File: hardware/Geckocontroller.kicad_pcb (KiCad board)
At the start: 2 copper layers, 114.3 x 96.5 mm, 103 parts, among them J101 AC Input, J11 I²C (BME280), J21 RGB LED, J31 DS18B20 I, J32 DS18B20 II, J40 FAN, J51 USB-C, J60 Load Cell Connector, J70 SPI / Addon Connector, J81 Dimmer, J91 Pump, J92 HeatBed, J93 HeatLamp, K81 AQG12212, K91 AQG12112, K92 AQG12112, K93 AQG12112, Q21 AO3400A, Q22 AO3400A, Q23 AO3400A, Q51 S8050, Q52 S8050, Q61 S8550, Q81 AO3400A, Q91 AO3400A, Q92 AO3400A, Q93 AO3400A, SW1 SW_Push, SW2 SW_Push, U1 ESP32-WROOM-32, U101 ACT4088, U2 CP2102, U61 HX711, U81 6N138

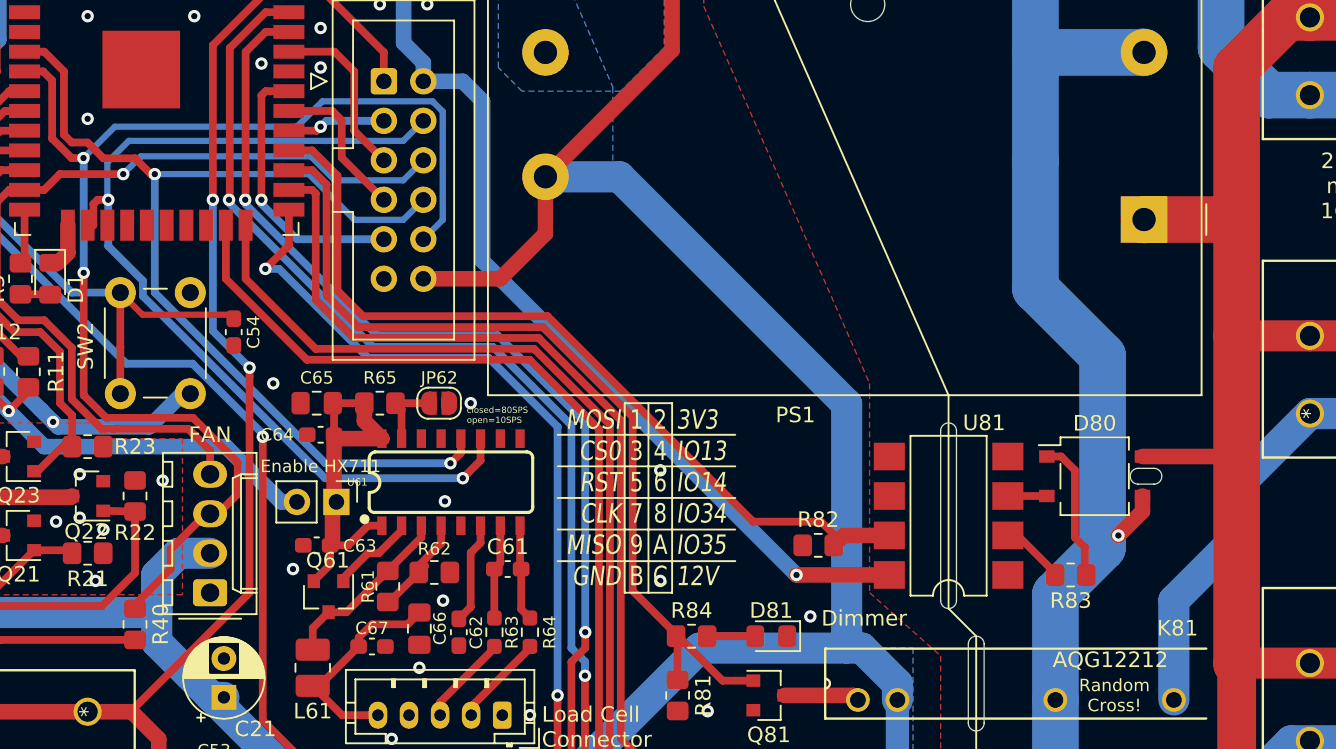
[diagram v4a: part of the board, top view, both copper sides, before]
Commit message: hardware: Improve Zero-Cross Detection circuit
Thanks to Patagona and LeoDJ!
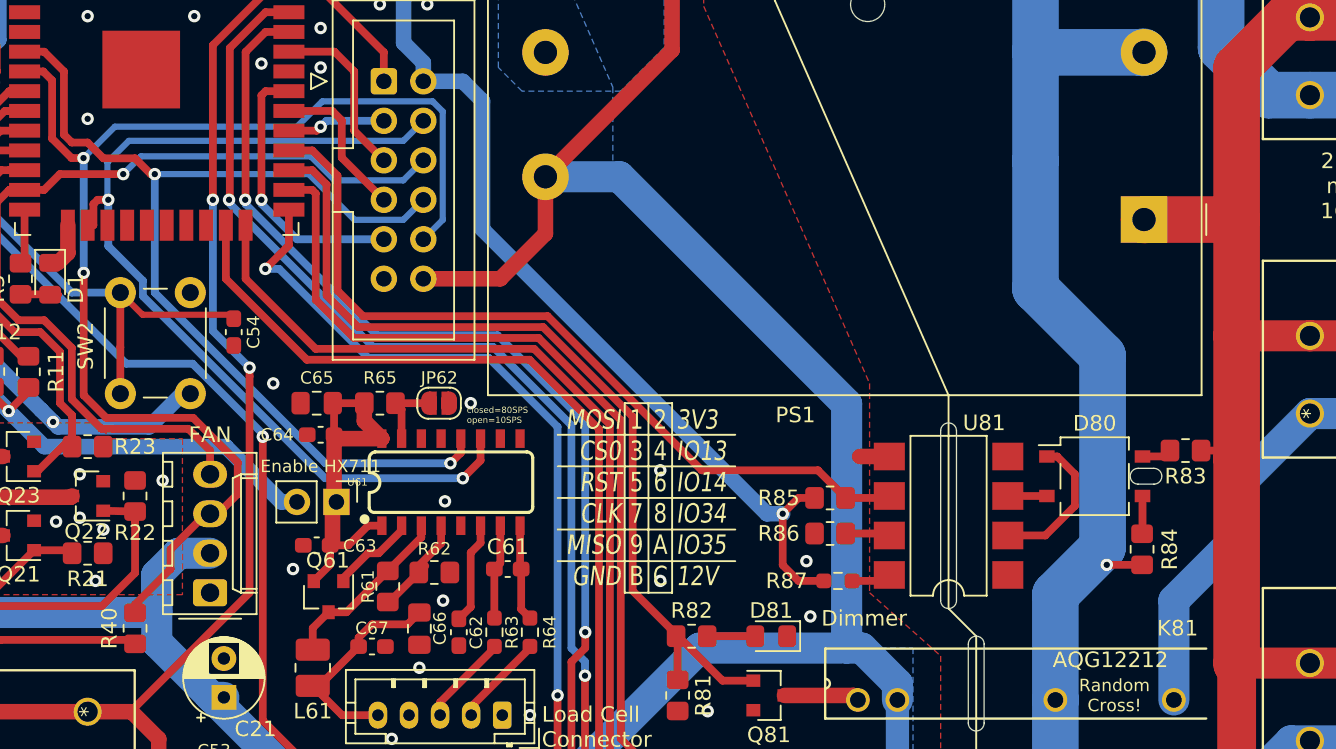
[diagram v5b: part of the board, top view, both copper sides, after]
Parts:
- removed the R82 at (80.0, 64.8)
- added R84: 160kR, Resistor_SMD:R_0805_2012Metric_Pad1.20x1.40mm_HandSolder, F.Cu at (100.8, 65.0)
- added R85: 12kR, Resistor_SMD:R_0805_2012Metric_Pad1.20x1.40mm_HandSolder, F.Cu at (80.8, 61.7)
- added R86: 100kR, Resistor_SMD:R_0805_2012Metric_Pad1.20x1.40mm_HandSolder, F.Cu at (80.8, 64.0)
- added R87: 100R, Resistor_SMD:R_0603_1608Metric_Pad0.98x0.95mm_HandSolder, F.Cu at (81.3, 67.1)
- R83: value 330kR -> 160kR
- moved R83 10.9 mm to (103.6, 58.7)
- moved R40 0.25 mm to (36.1, 70.1), turned to 90 degrees
- renumbered R84 to R82
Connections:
- D80 pad 3: /L' -> Net-(D80-Pad3)
- D80 pad 4: /N -> Net-(D80-Pad4)
- R40 pad 1: FAN_SIG -> +3V3
- R40 pad 2: +3V3 -> FAN_SIG
- R83 pad 1: Net-(D80-Pad1) -> /N
- R83 pad 2: Net-(R83-Pad2) -> Net-(D80-Pad4)
- U81 pad 2: Net-(R83-Pad2) -> Net-(D80-Pad1)
- U81 pad 5: Net-(U81-Pad5) -> GND
- U81 pad 6: Net-(U81-Pad6) -> /ZX_in
- U81 pad 7: /ZX_in -> Net-(R86-Pad2)
- U81 pad 8: +3V3 -> Net-(R87-Pad1)
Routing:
- net Net-(R83-Pad2): track 4.30 -> 0.00 mm
- net /N: track 136.3 -> 132.8 mm
- net Net-(R86-Pad2): track 0.00 -> 2.86 mm
- net Net-(R87-Pad1): track 0.00 -> 2.55 mm
- net Net-(D80-Pad3): track 0.00 -> 2.44 mm
- net Net-(D80-Pad4): track 0.00 -> 1.92 mm
- net GND: track 37.5 -> 39.4 mm, vias 72 -> 73
- net /ZX_in: track 54.1 -> 52.4 mm
- net /L': track 107.0 -> 106.1 mm
- net +3V3: track 302.9 -> 302.1 mm

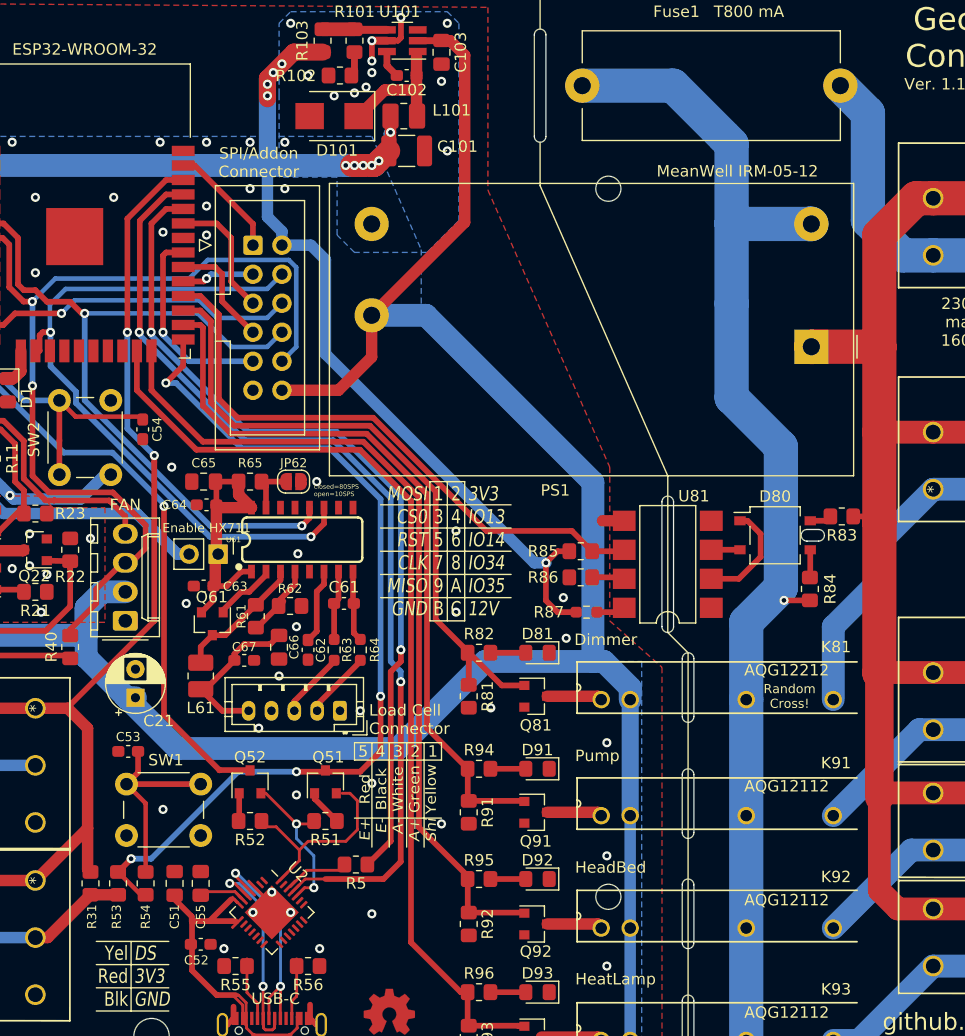
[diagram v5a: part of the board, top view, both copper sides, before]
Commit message: hardware: Change footprint of optocoupler
use a wider version, make it easier to solder
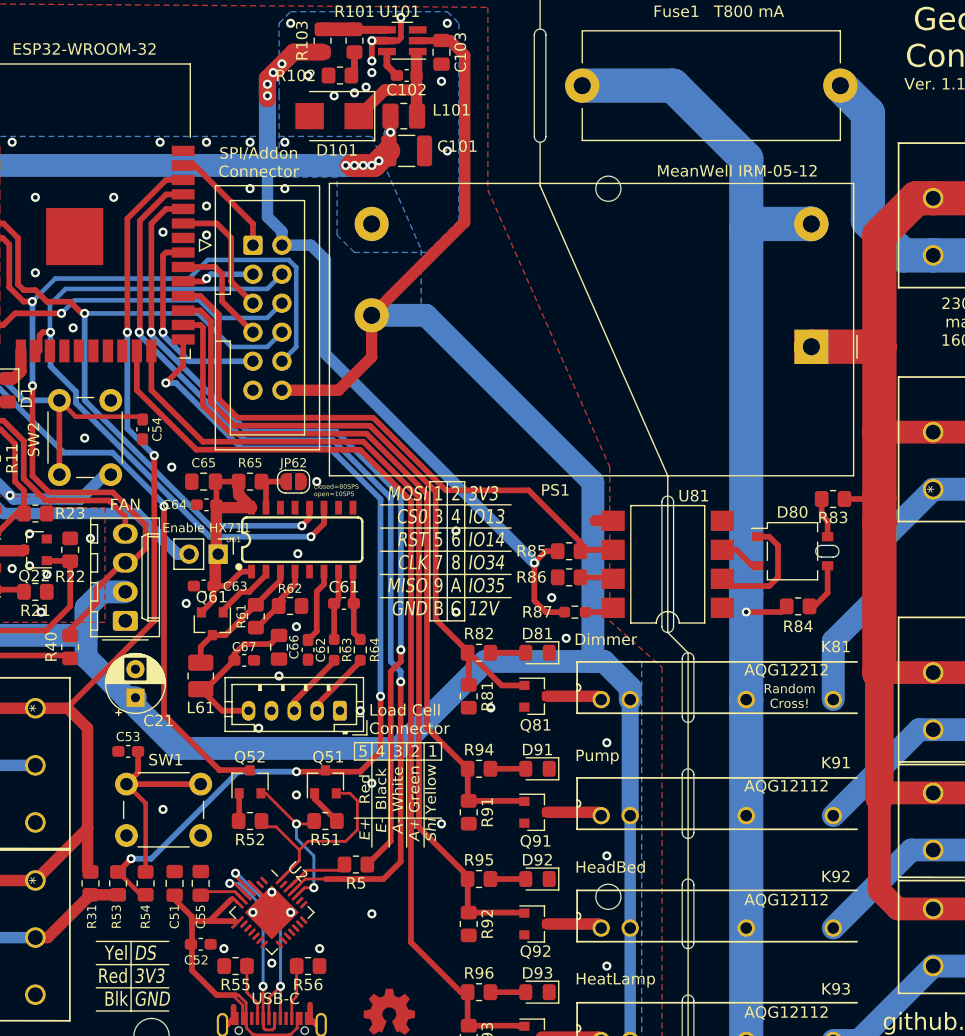
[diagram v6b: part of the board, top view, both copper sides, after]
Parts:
- R83, R84: value 160kR -> 160k
- R85: value 12kR -> 12k
- R86: value 100kR -> 100k
- U81: footprint Package_DIP:SMDIP-8_W7.62mm -> Package_DIP:SMDIP-8_W9.53mm
- moved D80 2.07 mm to (99.3, 61.7)
- moved R84 1.84 mm to (99.8, 66.5), turned to 0 degrees
- moved R83 1.70 mm to (102.9, 57.1)
- moved R85 1.02 mm to (79.8, 61.7)
- moved R86 1.02 mm to (79.8, 64.0)
- moved R87 1.02 mm to (80.3, 67.1)
- moved REF** 0.51 mm to (103.9, 58.2)
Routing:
- net /L': track 106.1 -> 104.0 mm
- net Net-(D80-Pad3): track 2.44 -> 4.45 mm
- net Net-(D80-Pad4): track 1.92 -> 3.52 mm
- net Net-(D80-Pad2): track 2.64 -> 3.66 mm
- net +3V3: track 302.1 -> 301.1 mm
- net Net-(D80-Pad1): track 9.42 -> 10.4 mm
- net /ZX_in: track 52.4 -> 51.8 mm
- net /N: track 132.8 -> 133.5 mm
- net GND: track 39.4 -> 39.1 mm, vias 73 -> 76
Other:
- outline, holes or cut-outs redrawn

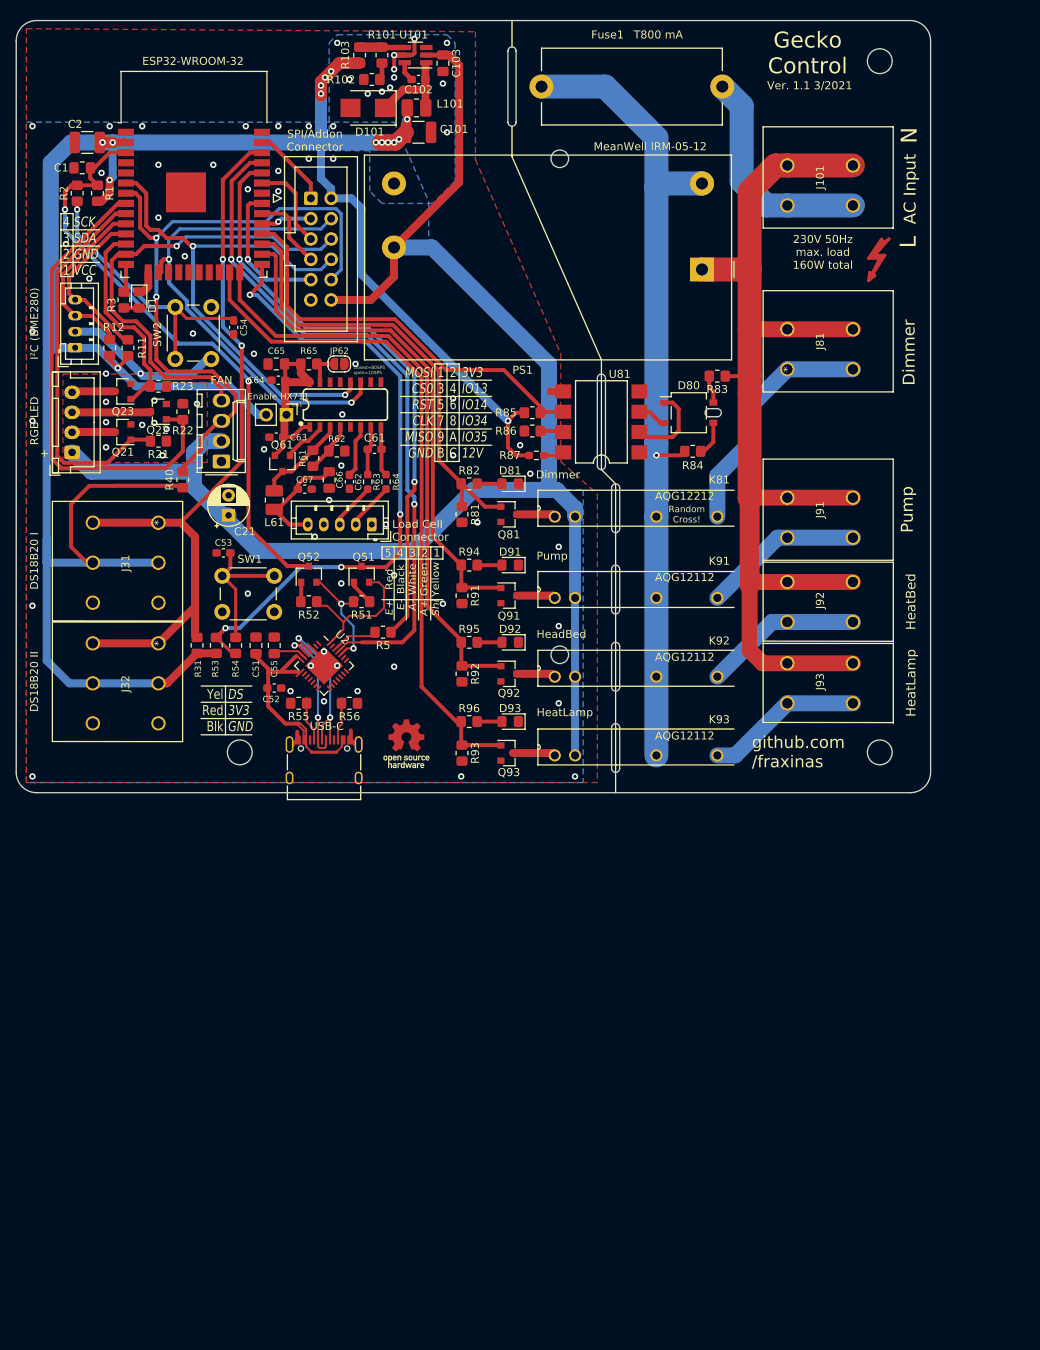
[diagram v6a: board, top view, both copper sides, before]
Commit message: PCB: Implement Fan PWM switch / rearrange modules
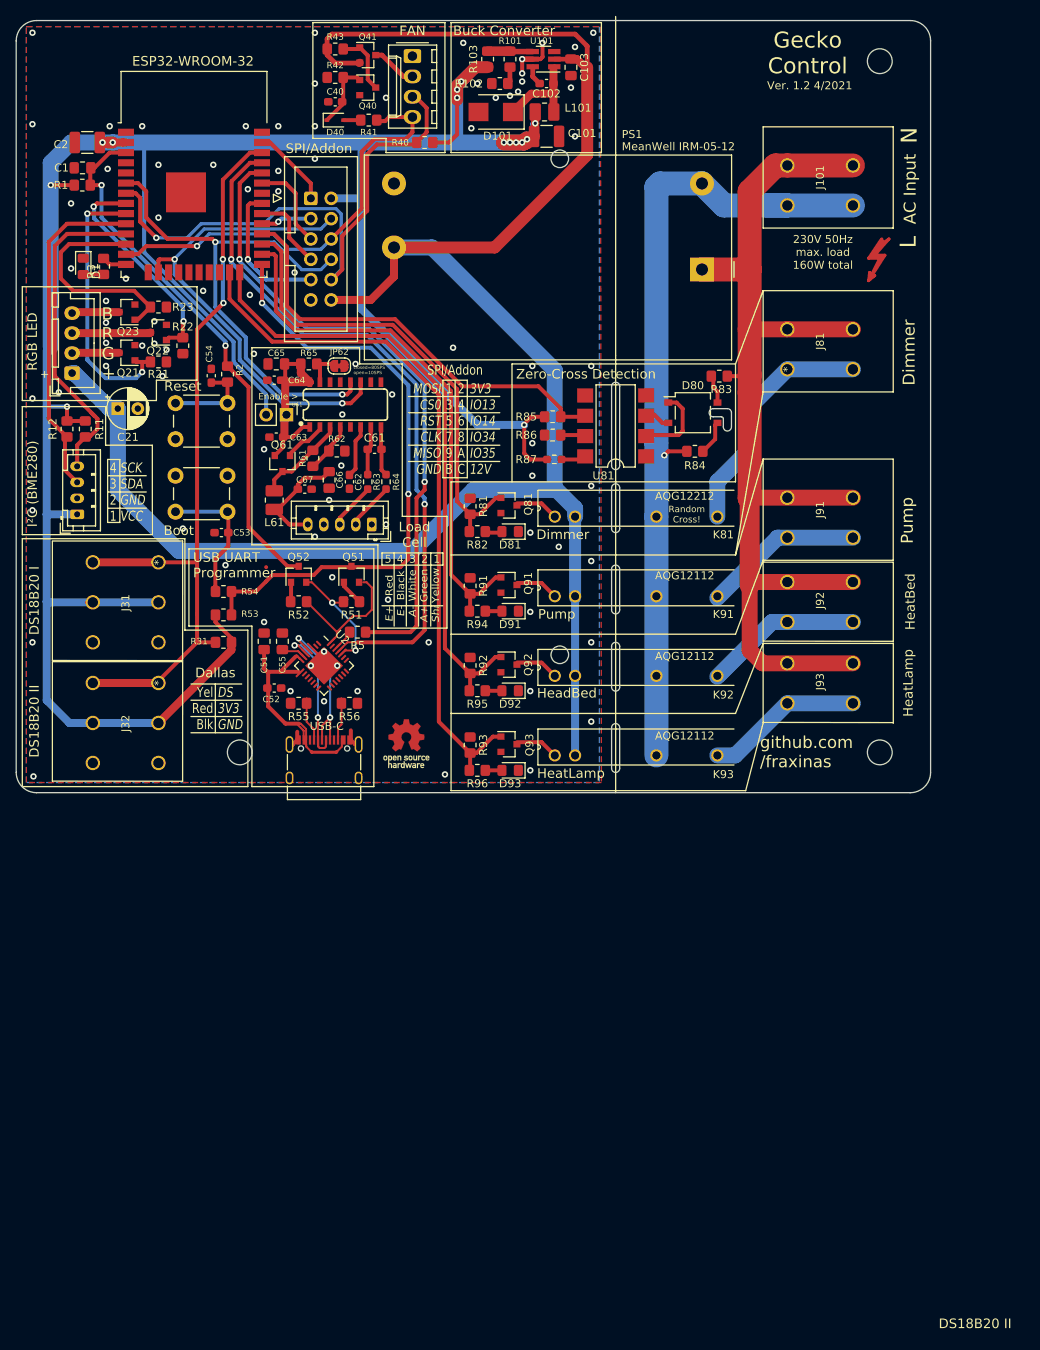
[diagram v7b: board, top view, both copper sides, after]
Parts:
- removed Fuse1: T800 mA, Fuse:Fuseholder_Cylinder-5x20mm_Stelvio-Kontek_PTF78_Horizontal_Open
- added ?: , , F.Cu at (41.4, 114.3)
- added C40: 22nF, Capacitor_SMD:C_0603_1608Metric_Pad1.08x0.95mm_HandSolder, F.Cu at (55.1, 22.9)
- added D40: 1N4148WS, Diode_SMD:D_SOD-323, F.Cu at (55.1, 25.1)
- added Q40: AO3400A, Package_TO_SOT_SMD:SOT-23, F.Cu at (59.2, 21.1)
- added Q41: AO3401A, Package_TO_SOT_SMD:SOT-23, F.Cu at (59.2, 17.0)
- added R41: 1k, Resistor_SMD:R_0805_2012Metric_Pad1.20x1.40mm_HandSolder, F.Cu at (59.3, 25.1)
- added R42: 160k, Resistor_SMD:R_0805_2012Metric_Pad1.20x1.40mm_HandSolder, F.Cu at (55.1, 19.8)
- added R43: 68k, Resistor_SMD:R_0805_2012Metric_Pad1.20x1.40mm_HandSolder, F.Cu at (55.1, 16.3)
- JP61: value Enable HX711 -> Enable >
- JP62: footprint Jumper:SolderJumper-2_P1.3mm_Open_RoundedPad1.0x1.5mm -> Jumper:SolderJumper-2_P1.3mm_Bridged_RoundedPad1.0x1.5mm
- SW1: value SW_Push -> Boot
- SW2: value SW_Push -> Reset
- U81: footprint Package_DIP:SMDIP-8_W9.53mm -> Package_DIP:SMDIP-8_W7.62mm
- moved J40 56.0 mm to (64.8, 17.1), turned to 270 degrees
- moved R40 51.9 mm to (66.3, 27.9), turned to 180 degrees
- moved R2 29.4 mm to (41.7, 56.9)
- moved SW1 21.0 mm to (35.2, 69.6), turned to 0 degrees
- moved J11 20.8 mm to (22.9, 74.4)
- moved C21 19.2 mm to (27.9, 61.2), turned to 0 degrees
- moved SW2 16.6 mm to (41.7, 65.0), turned to 180 degrees
- moved C101 16.0 mm to (81.5, 27.2)
- moved C102 16.0 mm to (81.5, 20.6)
- moved R103 16.0 mm to (74.2, 17.5)
- moved U101 16.0 mm to (81.2, 17.5)
- moved R101 16.0 mm to (77.0, 17.5)
- moved C103 16.0 mm to (84.6, 18.5)
- moved D101 16.0 mm to (75.2, 24.1)
- moved L101 16.0 mm to (81.3, 24.1)
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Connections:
- net /RXD0 renamed Net-(R5-Pad2)
- J40 pad 2: +12V -> /VFAN
- J51 pad A8: Net-(J51-PadA8) -> (no net)
- J51 pad B8: Net-(J51-PadB8) -> (no net)
- K81 pad O1: /L' -> /L
- K91 pad O1: /L' -> /L
- K92 pad O1: /L' -> /L
- K93 pad O1: /L' -> /L
- PS1 pad 2: /L' -> /L
- R84 pad 1: /L' -> /L
- U1 pad 17: Net-(U1-Pad17) -> (no net)
- U1 pad 18: Net-(U1-Pad18) -> (no net)
- U1 pad 19: Net-(U1-Pad19) -> (no net)
- U1 pad 20: Net-(U1-Pad20) -> (no net)
- U1 pad 21: Net-(U1-Pad21) -> (no net)
- U1 pad 22: Net-(U1-Pad22) -> (no net)
- U1 pad 32: Net-(U1-Pad32) -> (no net)
- U1 pad 4: Net-(U1-Pad4) -> (no net)
- U1 pad 5: Net-(U1-Pad5) -> (no net)
- U101 pad 3: Net-(U101-Pad3) -> (no net)
- U2 pad 1: Net-(U2-Pad1) -> (no net)
- U2 pad 10: Net-(U2-Pad10) -> (no net)
- U2 pad 11: Net-(U2-Pad11) -> (no net)
- U2 pad 12: Net-(U2-Pad12) -> (no net)
- U2 pad 13: Net-(U2-Pad13) -> (no net)
- U2 pad 14: Net-(U2-Pad14) -> (no net)
- U2 pad 15: Net-(U2-Pad15) -> (no net)
- U2 pad 16: Net-(U2-Pad16) -> (no net)
- U2 pad 17: Net-(U2-Pad17) -> (no net)
- U2 pad 18: Net-(U2-Pad18) -> (no net)
- U2 pad 19: Net-(U2-Pad19) -> (no net)
- U2 pad 2: Net-(U2-Pad2) -> (no net)
- U2 pad 20: Net-(U2-Pad20) -> (no net)
- U2 pad 21: Net-(U2-Pad21) -> (no net)
- U2 pad 22: Net-(U2-Pad22) -> (no net)
- U2 pad 23: Net-(U2-Pad23) -> (no net)
- U2 pad 27: Net-(U2-Pad27) -> (no net)
- U2 pad 9: Net-(U2-Pad9) -> (no net)
- U61 pad 10: Net-(U61-Pad10) -> (no net)
- U61 pad 13: Net-(U61-Pad13) -> (no net)
- U61 pad 9: Net-(U61-Pad9) -> (no net)
- U81 pad 1: Net-(U81-Pad1) -> (no net)
- U81 pad 4: Net-(U81-Pad4) -> (no net)
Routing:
- net /L': track 104.0 -> 0.00 mm, vias 1 -> 0
- net /L: track 28.0 -> 103.0 mm, vias 0 -> 1
- net +12V: track 197.8 -> 254.0 mm
- net /Red_out: track 60.1 -> 27.4 mm, vias 0 -> 2
- net +3V3: track 301.1 -> 329.1 mm, vias 15 -> 14
- net GND: track 39.1 -> 15.0 mm, vias 76 -> 88
- net /Reset_switch: track 34.4 -> 11.2 mm, vias 1 -> 0
- net /I2C_SDI: track 22.3 -> 42.6 mm
- net /I2C_SCK: track 21.2 -> 41.2 mm
- net /Green_out: track 48.5 -> 34.5 mm, vias 0 -> 2
- net FAN_SIG: track 82.0 -> 73.1 mm, vias 2 -> 1
- net Net-(C40-Pad2): track 0.00 -> 8.63 mm
- net EN: track 75.7 -> 67.6 mm
- net Net-(Q40-Pad3): track 0.00 -> 8.04 mm
- net /VFAN: track 0.00 -> 6.14 mm
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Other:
- outline, holes or cut-outs redrawn
- board text added: "B R G +"
- board text added: "Buck Converter"
- board text added: "Dallas"
- board text added: "Load Cell"
- board text added: "SPI/Addon"
- board text added: "USB UART Programmer"
- board text added: "Ver. 1.2 4/2021"
- board text added: "Zero-Cross Detection"
- board text removed: "Load Cell Connector"
- board text removed: "SPI/Addon Connector"
- board text removed: "Ver. 1.1 3/2021"
